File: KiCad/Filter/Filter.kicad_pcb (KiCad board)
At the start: 2 copper layers, 51 x 59 mm, 38 parts, among them J1 Screw_Terminal_01x03, J2 Screw_Terminal_01x03, U1 TL074

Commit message: preparation to merge project back into one board
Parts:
- renumbered R7 to R100
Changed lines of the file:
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@@
 			(plot_on_all_layers_selection 0x00000000_00000000_00000000_00000000)
 			(disableapertmacros no)
-			(usegerberextensions no)
+			(usegerberextensions yes)
 			(usegerberattributes yes)
 			(usegerberadvancedattributes yes)
-			(creategerberjobfile yes)
+			(creategerberjobfile no)
 			(dashed_line_dash_ratio 12)
 			(dashed_line_gap_ratio 3)
@@
 			(outputformat 1)
 			(mirror no)
-			(drillshape 1)
+			(drillshape 0)
 			(scaleselection 1)
-			(outputdirectory "")
+			(outputdirectory "../../Build/Aug 20 2026/")
 		)
 	)
@@
 		(at 85 98)
 		(property "Reference" "J1"
-			(at 0 -5.135 0)
+			(at -9 3.5 0)
 			(layer "F.SilkS")
 			(effects
@@
 		(at 102 98)
 		(property "Reference" "J2"
-			(at 0 -5.135 0)
+			(at 9 3.5 0)
 			(layer "F.SilkS")
 			(effects
@@
 		(descr "Resistor SMD 0805 (2012 Metric), square (rectangular) end terminal, IPC-7351 nominal, (Body size source: IPC-SM-782 page 72, https://www.pcb-3d.com/wordpress/wp-content/uploads/ipc-sm-782a_amendment_1_and_2.pdf)")
 		(tags "resistor")
-		(property "Reference" "R7"
+		(property "Reference" "R100"
 			(at 3 0 0)
 			(layer "F.SilkS")
@@
 		(layer "Edge.Cuts")
 	)
-	(gr_text "Neg\nOffset In"
-		(at 68 66 0)
+	(gr_text "+9V"
+		(at 96.5 93.5 0)
 		(layer "F.SilkS")
 		(effects
 			(font
-				(size 1.5 1.5)
-				(thickness 0.3)
+				(size 1 1)
+				(thickness 0.2)
 				(bold yes)
 			)
-			(justify left bottom)
+			(justify bottom)
 		)
 	)
-	(gr_text "-9V"
-		(at 111.5 78.75 0)
+	(gr_text "GND"
+		(at 102 93.5 0)
 		(layer "F.SilkS")
 		(effects
 			(font
-				(size 1.5 1.5)
-				(thickness 0.3)
+				(size 1 1)
+				(thickness 0.2)
 				(bold yes)
 			)
-			(justify left bottom)
+			(justify bottom)
 		)
 	)
-	(gr_text "+9V"
-		(at 111.5 86.25 0)
+	(gr_text "-9V"
+		(at 107 93.5 0)
 		(layer "F.SilkS")
 		(effects
 			(font
-				(size 1.5 1.5)
-				(thickness 0.3)
+				(size 1 1)
+				(thickness 0.2)
 				(bold yes)
 			)
-			(justify left bottom)
+			(justify bottom)
 		)
 	)
 	(gr_text "In"
-		(at 77 90 0)
+		(at 78.5 93.5 0)
 		(layer "F.SilkS")
 		(effects
 			(font
-				(size 1.5 1.5)
-				(thickness 0.3)
+				(size 1.2 1.2)
+				(thickness 0.24)
 				(bold yes)
 			)
@@
 	)
 	(gr_text "Control"
-		(at 85 87.25 0)
+		(at 85 93.5 0)
+		(layer "F.SilkS")
+		(effects
+			(font
+				(size 1.2 1.2)
+				(thickness 0.24)
+				(bold yes)
+			)
+			(justify bottom)
+		)
+	)
+	(gr_text "Out"
+		(at 91 93.5 0)
+		(layer "F.SilkS")
+		(effects
+			(font
+				(size 1.2 1.2)
+				(thickness 0.24)
+				(bold yes)
+			)
+			(justify bottom)
+		)
+	)
+	(gr_text "Neg\nOffset In"
+		(at 68 66 0)
 		(layer "F.SilkS")
 		(effects
@@
 				(bold yes)
 			)
-			(justify bottom)
+			(justify left bottom)
 		)
 	)
-	(gr_text "Inverted,    Raw Out"
-		(at 92.5 48.5 0)
+	(gr_text "-9V"
+		(at 111.5 78.75 0)
 		(layer "F.SilkS")
 		(effects
@@
 				(bold yes)
 			)
-			(justify bottom)
+			(justify left bottom)
 		)
 	)
-	(gr_text "Out"
-		(at 94 90 0)
+	(gr_text "+9V"
+		(at 111.5 86.25 0)
+		(layer "F.SilkS")
+		(effects
+			(font
+				(size 1.5 1.5)
+				(thickness 0.3)
+				(bold yes)
+			)
+			(justify left bottom)
+		)
+	)
+	(gr_text "Inverted,    Raw Out"
+		(at 92.5 48.5 0)
 		(layer "F.SilkS")
 		(effects

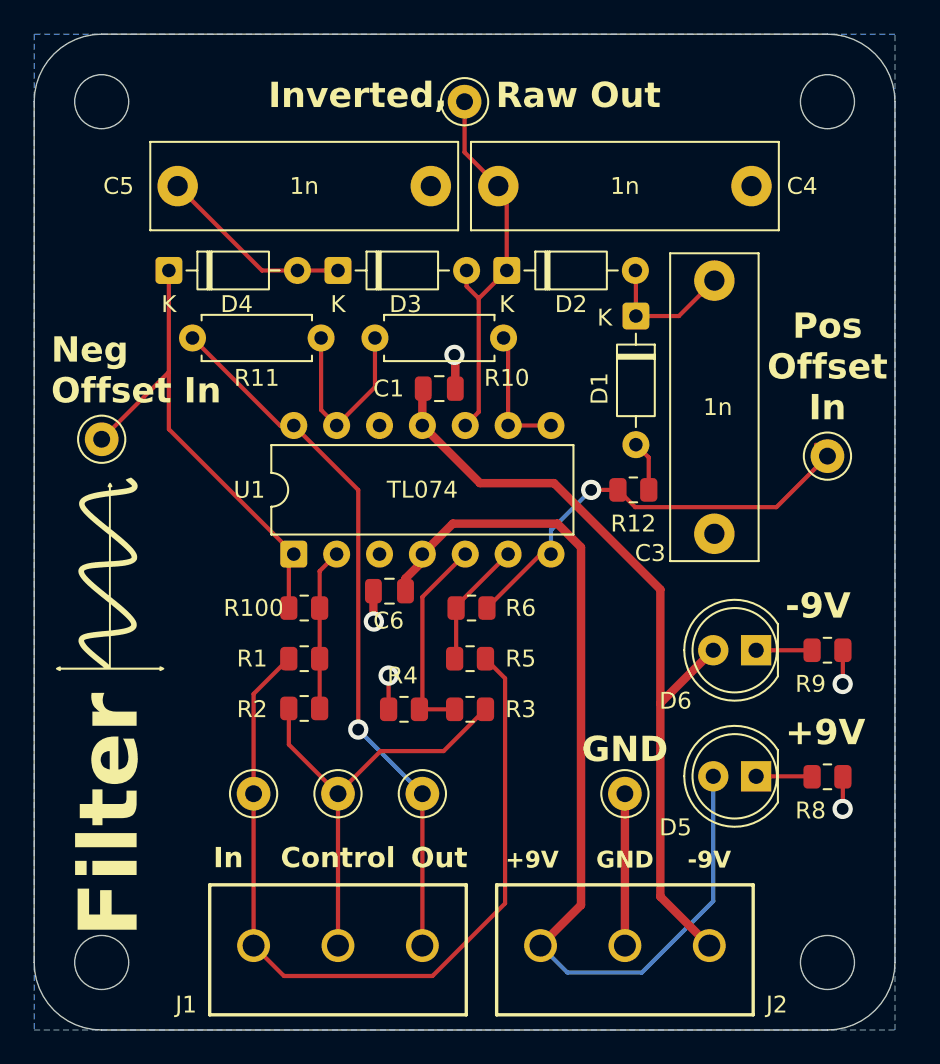
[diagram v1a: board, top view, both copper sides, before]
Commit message: merged project into one combined board (excluding the buttons)
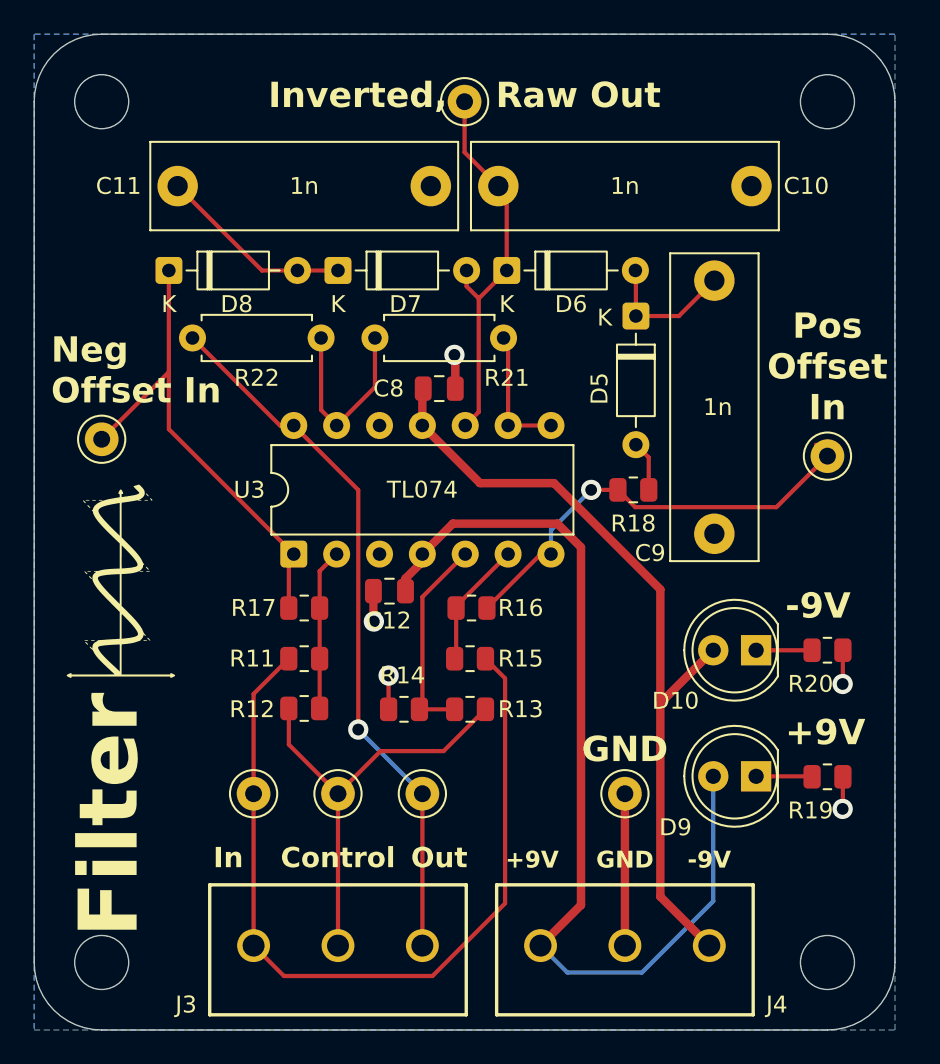
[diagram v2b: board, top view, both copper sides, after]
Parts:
- moved G*** 0.76 mm to (72.0, 75.0)
- renumbered C4 to C10, C5 to C11, C6 to C12, C1 to C8, C3 to C9, D6 to D10, D1 to D5, D2 to D6, D3 to D7, D4 to D8, D5 to D9, H1 to H5, H2 to H6, H4 to H7, H3 to H8, J1 to J3, J2 to J4, R1 to R11, R2 to R12, R3 to R13, R4 to R14, R5 to R15, R6 to R16, R100 to R17, R12 to R18, R8 to R19, R9 to R20, R10 to R21, R11 to R22, TP5 to TP10, TP6 to TP11, TP7 to TP12, TP1 to TP6, TP2 to TP7, TP3 to TP8, TP4 to TP9, U1 to U3
